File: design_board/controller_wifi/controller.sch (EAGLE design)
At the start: 58 parts, among them IC1 L293D, IC2 7805DT, IC4 7805TV

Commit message: Изменен модуль контроллера с wifi (добавлены конденсаторы на линии питания, резисторы на входе  - перед оптопарами)
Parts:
- added C1, C2, C3, C4: (no value), resistor:CPOL-EUE2.5-5
- added R10, R6, R7, R8, R9: (no value), resistor:R-EU_0204/2V
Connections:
- new net N$10: R8.2, X2-2.KL
- new net N$23: R7.2, X2-1.KL
- new net N$24: R9.2, X3-3.KL
- new net N$25: R10.2, X3-2.KL
- new net N$26: R6.2, X3-1.KL
- net +12V: now also C3.+
- net +3V3: now also C1.+
- net +5V: now also C2.+
- net GND: now also C1.-, C2.-, C3.-, C4.-
- net N$1: now also R9.1; no longer X3-2.KL
- net N$11: now also R10.1; no longer X3-1.KL
- net N$12: now also X1-4.KL; no longer X1-3.KL
- net N$14: now also X1-2.KL; no longer X1-1.KL
- net N$20: now also X1-1.KL; no longer X1-4.KL
- net N$21: now also X1-3.KL; no longer X1-2.KL
- net N$22: now also R6.1; no longer X2-2.KL
- net N$7: now also R7.1; no longer X2-1.KL
- net N$9: now also R8.1; no longer X3-3.KL
- net VCC/2: now also C4.+

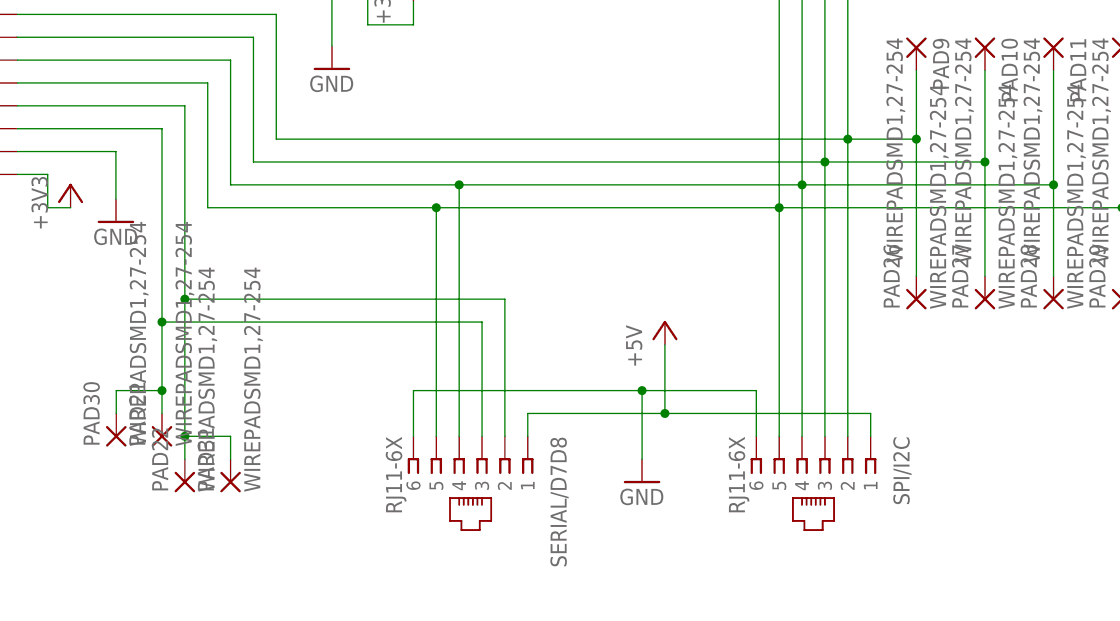
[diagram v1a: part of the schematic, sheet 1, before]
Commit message: Изменен модуль контроллера с wifi (заменены разъемы RJ-11, увеличина толщина дорожек), добавлены используемые библиотеки.
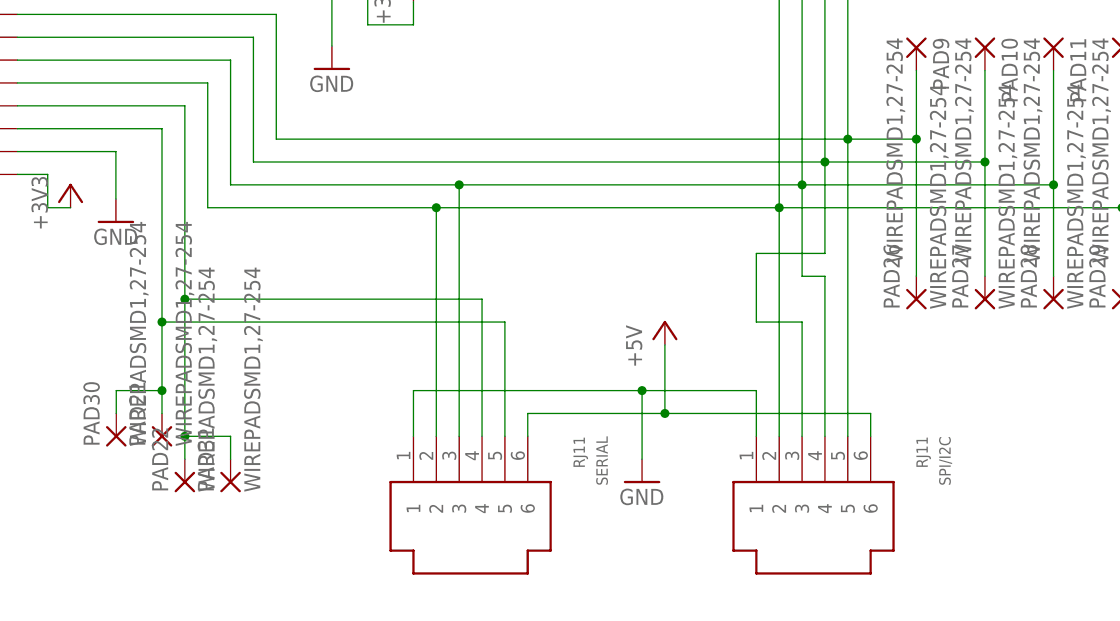
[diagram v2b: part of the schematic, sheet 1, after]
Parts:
- removed SERIAL/D7D8: RJ11-6X, con-tycoelectronics:RJ11-6X
- added SERIAL: RJ11, con-rj-11-6P6:RJ11
- SPI/I2C: value RJ11-6X -> RJ11; device con-tycoelectronics:RJ11-6X -> con-rj-11-6P6:RJ11
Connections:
- net +5V: now also SERIAL.6, SPI/I2C.6; no longer SERIAL/D7D8.1, SPI/I2C.1
- net GND: now also SERIAL.1, SPI/I2C.1; no longer SERIAL/D7D8.6, SPI/I2C.6
- net N$13: now also SERIAL.3; no longer SERIAL/D7D8.4
- net N$15: now also SERIAL.2, SPI/I2C.2; no longer SERIAL/D7D8.5, SPI/I2C.5
- net N$16: now also SERIAL.5; no longer SERIAL/D7D8.3
- net N$19: now also SPI/I2C.5; no longer SPI/I2C.2
- net N$8: now also SERIAL.4; no longer SERIAL/D7D8.2
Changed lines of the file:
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@@
 <part name="R4" library="resistor" deviceset="R-EU_" device="0204/5"/>
 <part name="R5" library="resistor" deviceset="R-EU_" device="0204/5"/>
-<part name="SPI/I2C" library="con-tycoelectronics" deviceset="RJ11" device="" technology="-6X"/>
 <part name="GND2" library="supply1" deviceset="GND" device=""/>
 <part name="P+3" library="supply1" deviceset="+5V" device=""/>
@@
 <part name="X2" library="con-wago-500" deviceset="W237-102" device=""/>
 <part name="X3" library="con-wago-500" deviceset="W237-103" device=""/>
-<part name="SERIAL/D7D8" library="con-tycoelectronics" deviceset="RJ11" device="" technology="-6X"/>
 <part name="P+7" library="supply1" deviceset="+5V" device=""/>
 <part name="P+8" library="supply1" deviceset="+12V" device=""/>
@@
 <part name="C4" library="resistor" deviceset="CPOL-EU" device="E2.5-5"/>
 <part name="P+13" library="supply1" deviceset="VCC/2" device=""/>
+<part name="SERIAL" library="con-rj-11-6P6" deviceset="RJ11" device=""/>
+<part name="SPI/I2C" library="con-rj-11-6P6" deviceset="RJ11" device=""/>
 </parts>
 <sheets>
@@
 <instance part="R4" gate="G$1" x="50.8" y="22.86" rot="R270"/>
 <instance part="R5" gate="G$1" x="35.56" y="22.86" rot="R270"/>
-<instance part="SPI/I2C" gate="G$1" x="119.38" y="-66.04" rot="R270"/>
 <instance part="GND2" gate="1" x="99.06" y="-68.58"/>
 <instance part="P+3" gate="1" x="175.26" y="55.88"/>
@@
 <instance part="X3" gate="-2" x="83.82" y="83.82" rot="R270"/>
 <instance part="X3" gate="-3" x="78.74" y="83.82" rot="R270"/>
-<instance part="SERIAL/D7D8" gate="G$1" x="81.28" y="-66.04" rot="R270"/>
 <instance part="P+7" gate="1" x="101.6" y="-50.8"/>
 <instance part="P+8" gate="1" x="-11.26" y="-38.2"/>
@@
 <instance part="R9" gate="G$1" x="78.74" y="73.66" rot="R90"/>
 <instance part="R10" gate="G$1" x="83.82" y="73.66" rot="R90"/>
+<instance part="SERIAL" gate="G$1" x="81.28" y="-73.66" rot="R270"/>
+<instance part="SPI/I2C" gate="G$1" x="119.38" y="-73.66" rot="R270"/>
 </instances>
 <busses>
@@
 </segment>
 <segment>
-<pinref part="SPI/I2C" gate="G$1" pin="6"/>
 <wire x1="111.76" y1="-63.5" x2="111.76" y2="-58.42" width="0.1524" layer="91"/>
-<pinref part="SERIAL/D7D8" gate="G$1" pin="6"/>
 <wire x1="73.66" y1="-63.5" x2="73.66" y2="-58.42" width="0.1524" layer="91"/>
 <wire x1="73.66" y1="-58.42" x2="99.06" y2="-58.42" width="0.1524" layer="91"/>
@@
 <wire x1="99.06" y1="-66.04" x2="99.06" y2="-58.42" width="0.1524" layer="91"/>
 <junction x="99.06" y="-58.42"/>
+<pinref part="SPI/I2C" gate="G$1" pin="1"/>
+<pinref part="SERIAL" gate="G$1" pin="1"/>
 </segment>
 <segment>
@@
 </segment>
 <segment>
-<pinref part="SPI/I2C" gate="G$1" pin="1"/>
 <wire x1="124.46" y1="-60.96" x2="124.46" y2="-63.5" width="0.1524" layer="91"/>
-<pinref part="SERIAL/D7D8" gate="G$1" pin="1"/>
 <wire x1="86.36" y1="-63.5" x2="86.36" y2="-60.96" width="0.1524" layer="91"/>
 <wire x1="86.36" y1="-60.96" x2="101.6" y2="-60.96" width="0.1524" layer="91"/>
@@
 <wire x1="101.6" y1="-53.34" x2="101.6" y2="-60.96" width="0.1524" layer="91"/>
 <junction x="101.6" y="-60.96"/>
+<pinref part="SPI/I2C" gate="G$1" pin="6"/>
+<pinref part="SERIAL" gate="G$1" pin="6"/>
 </segment>
 </net>
@@
 <wire x1="29.64" y1="-21.7" x2="53.34" y2="-21.7" width="0.1524" layer="91"/>
 <wire x1="53.34" y1="-21.7" x2="53.34" y2="-35.56" width="0.1524" layer="91"/>
-<pinref part="SPI/I2C" gate="G$1" pin="4"/>
 <wire x1="53.34" y1="-35.56" x2="78.74" y2="-35.56" width="0.1524" layer="91"/>
 <wire x1="78.74" y1="-35.56" x2="116.84" y2="-35.56" width="0.1524" layer="91"/>
-<wire x1="116.84" y1="-35.56" x2="116.84" y2="-63.5" width="0.1524" layer="91"/>
 <pinref part="IC1" gate="G$1" pin="2A"/>
 <wire x1="137.16" y1="17.78" x2="116.84" y2="17.78" width="0.1524" layer="91"/>
@@
 <wire x1="144.78" y1="-45.72" x2="144.78" y2="-35.56" width="0.1524" layer="91"/>
 <junction x="144.78" y="-35.56"/>
-<pinref part="SERIAL/D7D8" gate="G$1" pin="4"/>
 <wire x1="78.74" y1="-63.5" x2="78.74" y2="-35.56" width="0.1524" layer="91"/>
 <junction x="78.74" y="-35.56"/>
+<pinref part="SERIAL" gate="G$1" pin="3"/>
+<wire x1="116.84" y1="-35.56" x2="116.84" y2="-45.72" width="0.1524" layer="91"/>
+<pinref part="SPI/I2C" gate="G$1" pin="4"/>
+<wire x1="116.84" y1="-45.72" x2="119.38" y2="-45.72" width="0.1524" layer="91"/>
+<wire x1="119.38" y1="-45.72" x2="119.38" y2="-63.5" width="0.1524" layer="91"/>
 </segment>
 </net>
@@
 <wire x1="29.64" y1="-24.24" x2="50.8" y2="-24.24" width="0.1524" layer="91"/>
 <wire x1="50.8" y1="-24.24" x2="50.8" y2="-38.1" width="0.1524" layer="91"/>
-<pinref part="SPI/I2C" gate="G$1" pin="5"/>
 <wire x1="50.8" y1="-38.1" x2="76.2" y2="-38.1" width="0.1524" layer="91"/>
 <wire x1="76.2" y1="-38.1" x2="114.3" y2="-38.1" width="0.1524" layer="91"/>
@@
 <wire x1="152.4" y1="-45.72" x2="152.4" y2="-38.1" width="0.1524" layer="91"/>
 <junction x="152.4" y="-38.1"/>
-<pinref part="SERIAL/D7D8" gate="G$1" pin="5"/>
 <wire x1="76.2" y1="-63.5" x2="76.2" y2="-38.1" width="0.1524" layer="91"/>
 <junction x="76.2" y="-38.1"/>
+<pinref part="SPI/I2C" gate="G$1" pin="2"/>
+<pinref part="SERIAL" gate="G$1" pin="2"/>
 </segment>
 </net>
@@
 <wire x1="29.64" y1="-26.78" x2="48.26" y2="-26.78" width="0.1524" layer="91"/>
 <wire x1="48.26" y1="-26.78" x2="48.26" y2="-48.26" width="0.1524" layer="91"/>
-<wire x1="48.26" y1="-48.26" x2="83.82" y2="-48.26" width="0.1524" layer="91"/>
 <pinref part="PAD22" gate="G$1" pin="P"/>
+<pinref part="PAD31" gate="G$1" pin="P"/>
 <wire x1="48.26" y1="-48.26" x2="48.26" y2="-63.5" width="0.1524" layer="91"/>
-<junction x="48.26" y="-48.26"/>
-<pinref part="PAD31" gate="G$1" pin="P"/>
 <wire x1="48.26" y1="-63.5" x2="48.26" y2="-66.04" width="0.1524" layer="91"/>
 <wire x1="53.34" y1="-66.04" x2="53.34" y2="-63.5" width="0.1524" layer="91"/>
 <wire x1="53.34" y1="-63.5" x2="48.26" y2="-63.5" width="0.1524" layer="91"/>
 <junction x="48.26" y="-63.5"/>
-<pinref part="SERIAL/D7D8" gate="G$1" pin="2"/>
-<wire x1="83.82" y1="-48.26" x2="83.82" y2="-63.5" width="0.1524" layer="91"/>
+<pinref part="SERIAL" gate="G$1" pin="4"/>
+<wire x1="81.28" y1="-63.5" x2="81.28" y2="-48.26" width="0.1524" layer="91"/>
+<wire x1="81.28" y1="-48.26" x2="48.26" y2="-48.26" width="0.1524" layer="91"/>
+<junction x="48.26" y="-48.26"/>
 </segment>
 </net>
@@
 <wire x1="29.64" y1="-29.32" x2="45.72" y2="-29.32" width="0.1524" layer="91"/>
 <wire x1="45.72" y1="-29.32" x2="45.72" y2="-50.8" width="0.1524" layer="91"/>
-<wire x1="45.72" y1="-50.8" x2="81.28" y2="-50.8" width="0.1524" layer="91"/>
+<wire x1="45.72" y1="-50.8" x2="83.82" y2="-50.8" width="0.1524" layer="91"/>
 <pinref part="PAD21" gate="G$1" pin="P"/>
 <wire x1="45.72" y1="-50.8" x2="45.72" y2="-58.42" width="0.1524" layer="91"/>
@@
 <wire x1="40.64" y1="-58.42" x2="45.72" y2="-58.42" width="0.1524" layer="91"/>
 <junction x="45.72" y="-58.42"/>
-<pinref part="SERIAL/D7D8" gate="G$1" pin="3"/>
-<wire x1="81.28" y1="-50.8" x2="81.28" y2="-63.5" width="0.1524" layer="91"/>
+<pinref part="SERIAL" gate="G$1" pin="5"/>
+<wire x1="83.82" y1="-50.8" x2="83.82" y2="-63.5" width="0.1524" layer="91"/>
 </segment>
 </net>
@@
 <wire x1="29.64" y1="-19.16" x2="55.88" y2="-19.16" width="0.1524" layer="91"/>
 <wire x1="55.88" y1="-19.16" x2="55.88" y2="-33.02" width="0.1524" layer="91"/>
-<pinref part="SPI/I2C" gate="G$1" pin="3"/>
 <wire x1="55.88" y1="-33.02" x2="119.38" y2="-33.02" width="0.1524" layer="91"/>
-<wire x1="119.38" y1="-33.02" x2="119.38" y2="-63.5" width="0.1524" layer="91"/>
 <wire x1="119.38" y1="12.7" x2="119.38" y2="-33.02" width="0.1524" layer="91"/>
 <junction x="119.38" y="-33.02"/>
@@
 <wire x1="137.16" y1="-45.72" x2="137.16" y2="-33.02" width="0.1524" layer="91"/>
 <junction x="137.16" y="-33.02"/>
+<pinref part="SPI/I2C" gate="G$1" pin="3"/>
+<wire x1="116.84" y1="-63.5" x2="116.84" y2="-50.8" width="0.1524" layer="91"/>
+<wire x1="116.84" y1="-50.8" x2="111.76" y2="-50.8" width="0.1524" layer="91"/>
+<wire x1="111.76" y1="-50.8" x2="111.76" y2="-43.18" width="0.1524" layer="91"/>
+<wire x1="111.76" y1="-43.18" x2="119.38" y2="-43.18" width="0.1524" layer="91"/>
+<wire x1="119.38" y1="-43.18" x2="119.38" y2="-33.02" width="0.1524" layer="91"/>
 </segment>
 </net>
@@
 <wire x1="167.64" y1="43.18" x2="180.34" y2="43.18" width="0.1524" layer="91"/>
 <wire x1="180.34" y1="43.18" x2="180.34" y2="2.54" width="0.1524" layer="91"/>
-<pinref part="SPI/I2C" gate="G$1" pin="2"/>
 <wire x1="121.92" y1="-63.5" x2="121.92" y2="-30.48" width="0.1524" layer="91"/>
 <pinref part="NODE_MCU_V1.0" gate="G$1" pin="D5"/>
@@
 <wire x1="129.54" y1="-45.72" x2="129.54" y2="-30.48" width="0.1524" layer="91"/>
 <junction x="129.54" y="-30.48"/>
-</segment>
-</net>
+<pinref part="SPI/I2C" gate="G$1" pin="5"/>
+</segment>
+</net>
